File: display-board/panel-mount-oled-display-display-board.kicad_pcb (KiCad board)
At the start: 2 copper layers, 40.7 x 21.1 mm, 32 parts, among them J1 Conn_01x08_Pin, J2 Conn_01x08_Pin, U1 XC6206PxxxMR

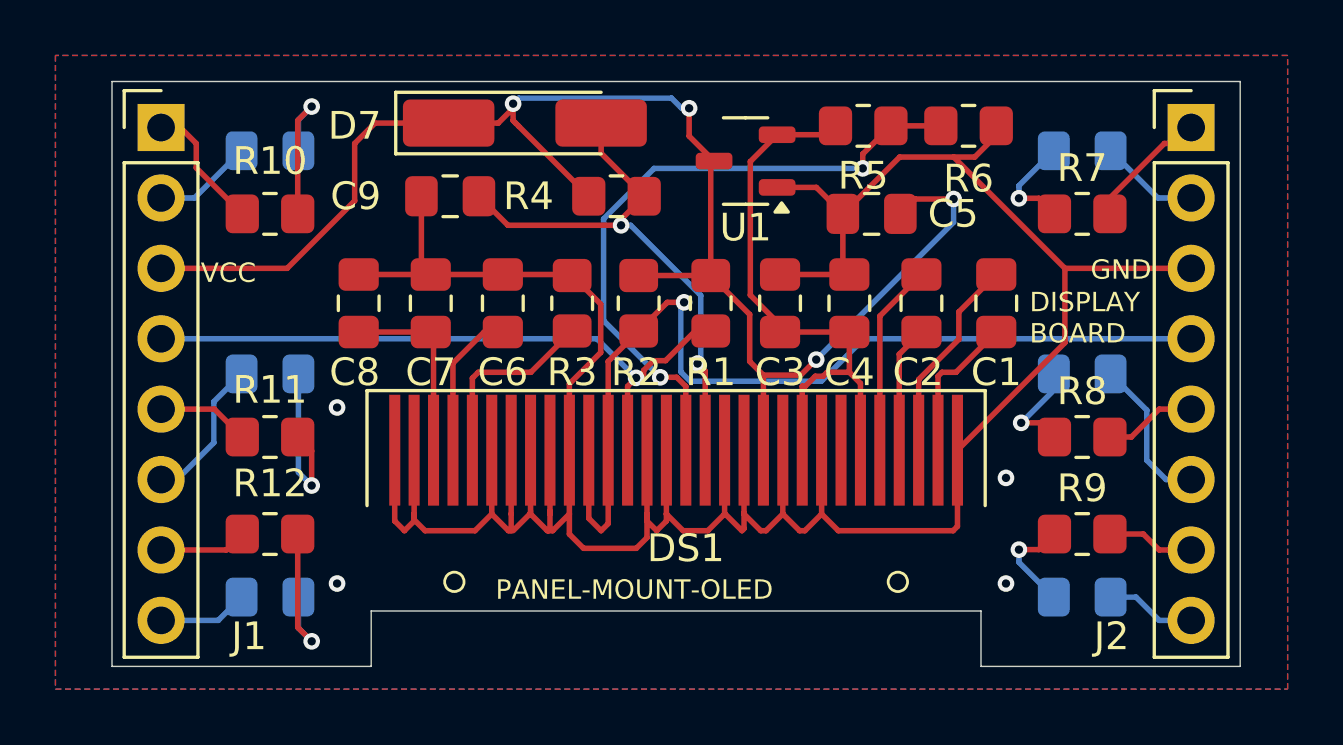
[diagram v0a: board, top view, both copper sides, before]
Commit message: display: widen PCB cutout and reposition LEDs clear of bezel
Expand the display mounting area slightly to fit marginally wider
OLED modules, and shift the status LEDs so they are not obstructed
by the panel bezel.
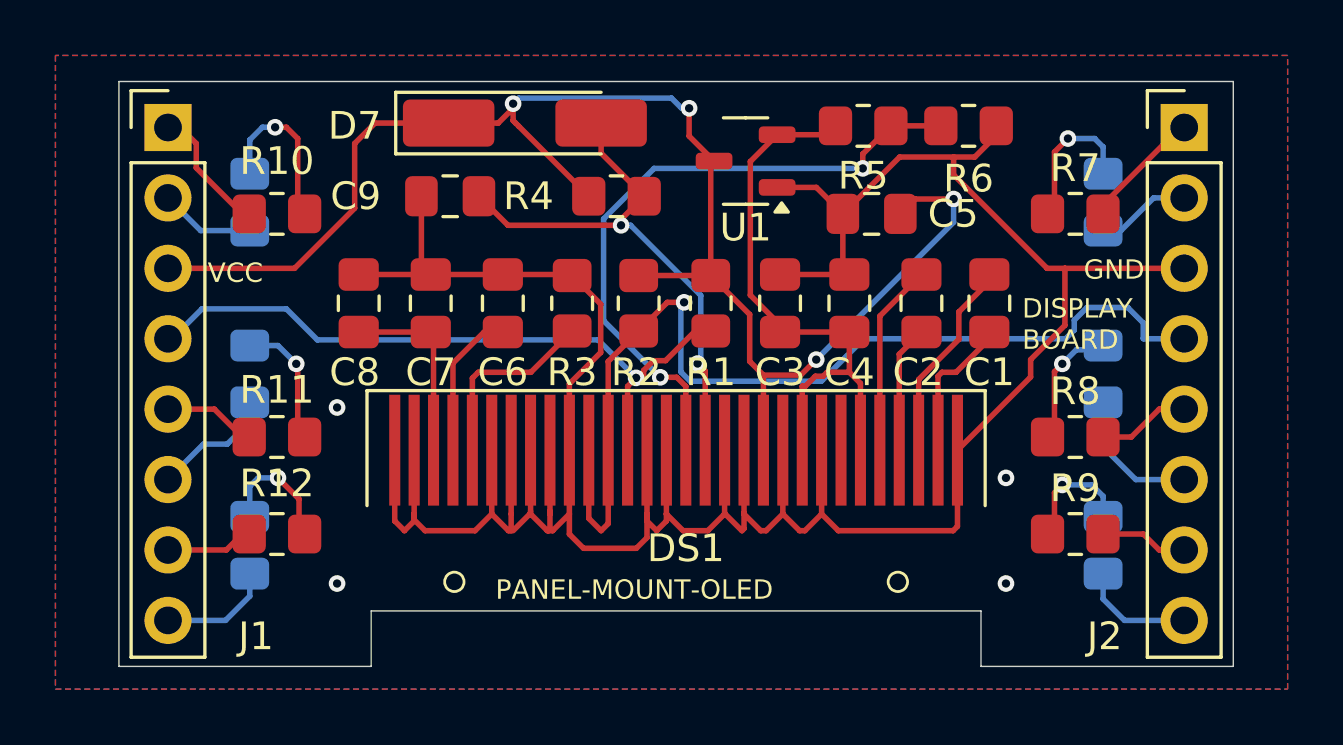
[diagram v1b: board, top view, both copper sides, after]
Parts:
- moved D3 2.02 mm to (136.9, 116.7), turned to -90 degrees
- moved D6 2.01 mm to (106.1, 116.7), turned to -90 degrees
- moved D1 2.00 mm to (136.9, 104.4), turned to -90 degrees
- moved D4 1.99 mm to (106.1, 104.4), turned to -90 degrees
- moved D2 0.76 mm to (136.9, 110.5), turned to -90 degrees
- moved D5 0.73 mm to (106.1, 110.5), turned to -90 degrees
- moved C1 0.25 mm to (132.8, 108.0)
- moved J1 0.25 mm to (103.1, 101.7)
- moved J2 0.25 mm to (139.8, 101.7)
- moved R10 0.25 mm to (107.0, 104.8)
- moved R11 0.25 mm to (107.0, 112.8)
- moved R12 0.25 mm to (107.0, 116.3)
- moved R7 0.25 mm to (135.8, 104.8)
- moved R8 0.25 mm to (135.8, 112.8)
- moved R9 0.25 mm to (135.8, 116.3)
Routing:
- net Net-(D5-K): track 6.18 -> 4.61 mm
- net Net-(D1-K): track 3.75 -> 5.28 mm
- net /SDA: track 35.3 -> 36.8 mm
- net Net-(D6-K): track 5.87 -> 4.60 mm
- net /D3A: track 3.25 -> 4.16 mm
- net /SCL: track 24.0 -> 24.9 mm
- net /D6A: track 3.25 -> 4.12 mm
- net Net-(D3-K): track 3.75 -> 4.27 mm
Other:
- board size 40.7 x 21.1 mm -> 40.2 x 21.1 mm
- board text added: "PANEL MNT OLED"
- board text removed: "PANEL MOUNT OLED"
